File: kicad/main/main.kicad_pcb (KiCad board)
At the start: 2 copper layers, 39 x 35 mm, 17 parts, among them J3 Conn_01x07_Pin, J4 Conn_01x04_Pin, P1 USB_C_Plug_USB2.0, SW3 SW_Push, SW4 SW_Push, U1 HUSB237

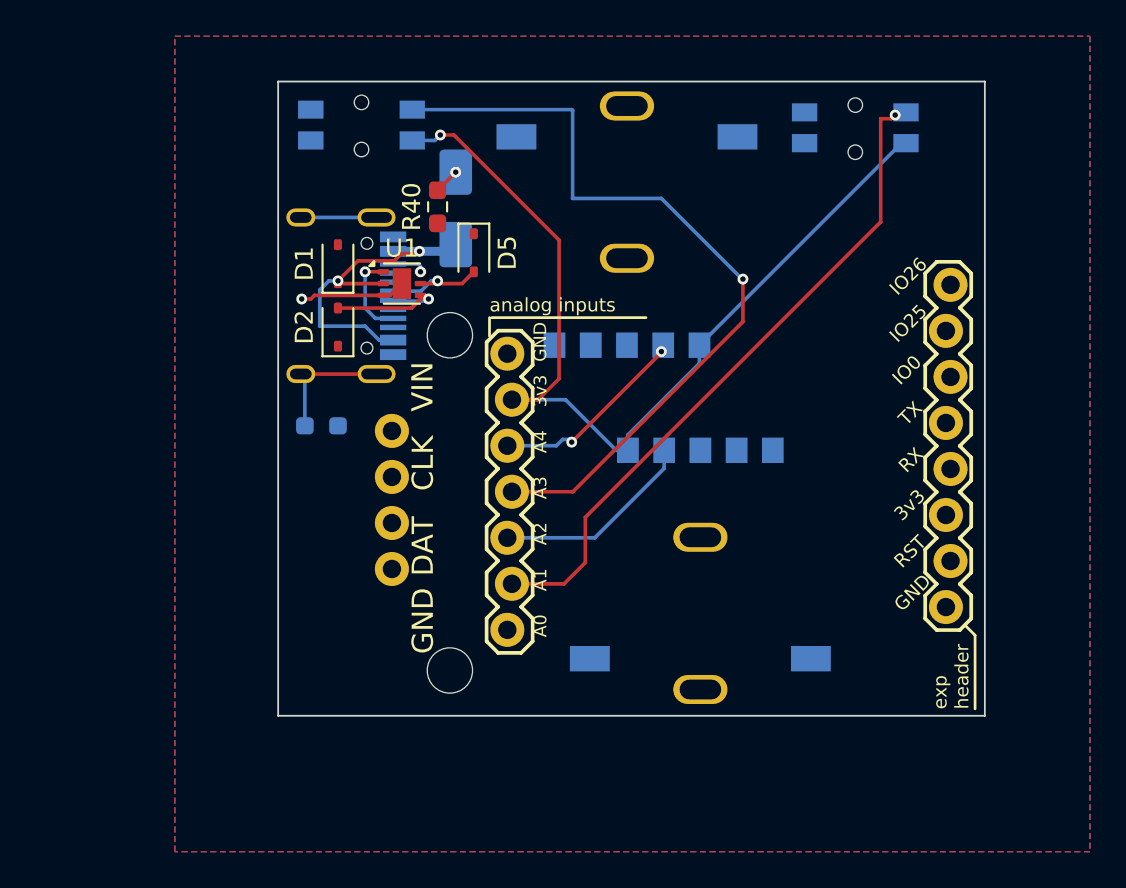
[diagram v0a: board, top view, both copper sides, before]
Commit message: Switches added
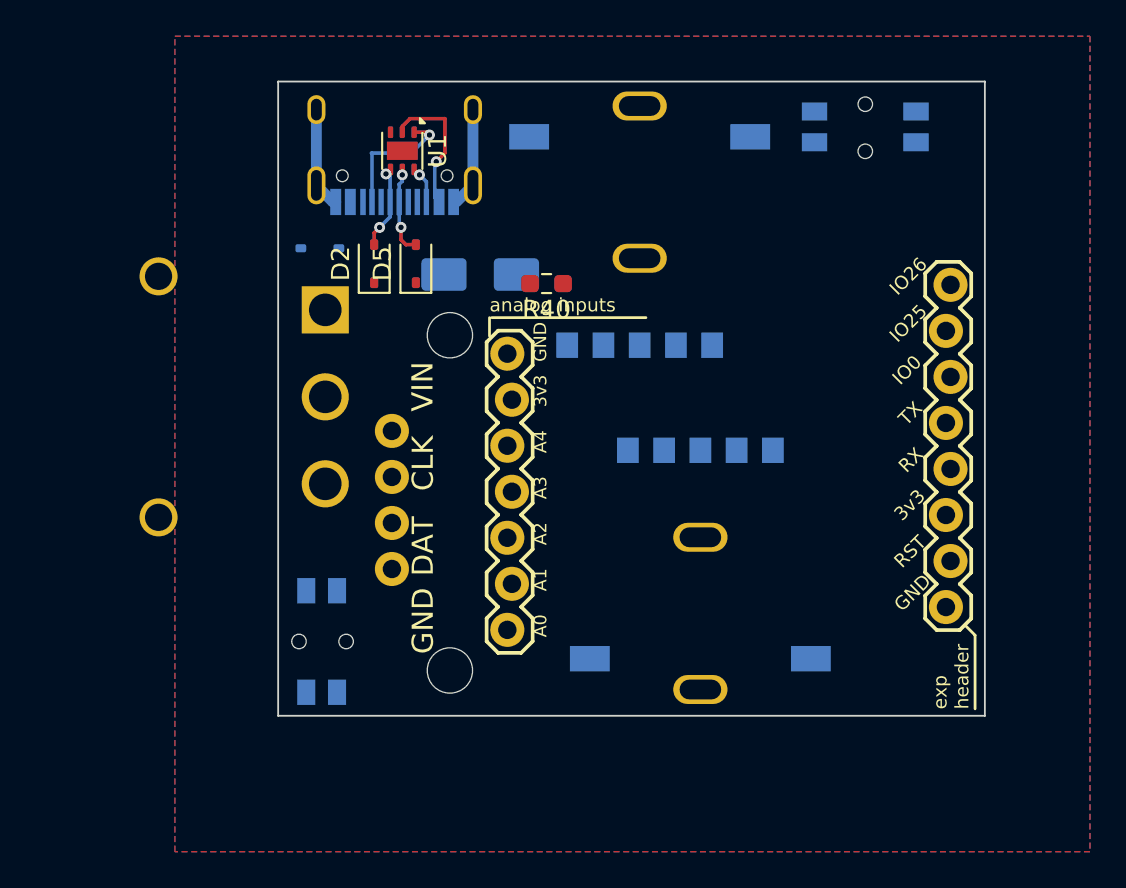
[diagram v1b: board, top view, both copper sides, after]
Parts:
- removed R39: 1M, Resistor_SMD:R_0603_1608Metric_Pad0.98x0.95mm_HandSolder
- added SW1: K3-1391B-51, easyeda2kicad:SW-TH_K3-1391B-51, B.Cu at (164.7, 92.4)
- D1: moved to B.Cu
- moved SW4 28.5 mm to (169.1, 105.9), turned to 90 degrees
- moved P1 10.1 mm to (173.1, 77.6), turned to 0 degrees
- moved R40 7.36 mm to (181.5, 86.2), turned to 180 degrees
- moved U1 7.33 mm to (173.6, 78.8), turned to -90 degrees
- moved D2 4.03 mm to (172.0, 85.0)
- moved D3 3.89 mm to (177.8, 85.7), turned to 0 degrees
- moved D5 3.26 mm to (174.3, 85.0), turned to 90 degrees
- moved D1 1.31 mm to (169.0, 84.2), turned to 180 degrees
- moved R1 0.70 mm to (186.7, 83.0)
- moved SW3 0.55 mm to (199.1, 77.5)
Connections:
- D3 pad 1: VIN -> VBUS
- D3 pad 2: VBUS -> Net-(D3-A)
- P1 pad S1: Net-(P1-SHIELD) -> GND
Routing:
- net +3V3: track 52.4 -> 0.00 mm, vias 1 -> 0
- net AIN3: track 43.9 -> 0.00 mm, vias 1 -> 0
- net AIN1: track 37.3 -> 0.00 mm, vias 1 -> 0
- net Net-(P1-SHIELD): track 11.3 -> 0.00 mm
- net AIN2: track 11.2 -> 0.00 mm
- net VBUS: track 18.9 -> 7.81 mm, vias 2 -> 1
- net AIN4: track 10.8 -> 0.00 mm, vias 2 -> 0
- net GND: track 5.88 -> 11.3 mm, vias 1 -> 0
- net D+: track 7.52 -> 4.80 mm, vias 1 -> 2
- net CC1: track 4.78 -> 7.24 mm
- net VIN: track 1.41 -> 0.00 mm, vias 1 -> 0
- net D-: track 5.91 -> 4.92 mm, vias 1 -> 2

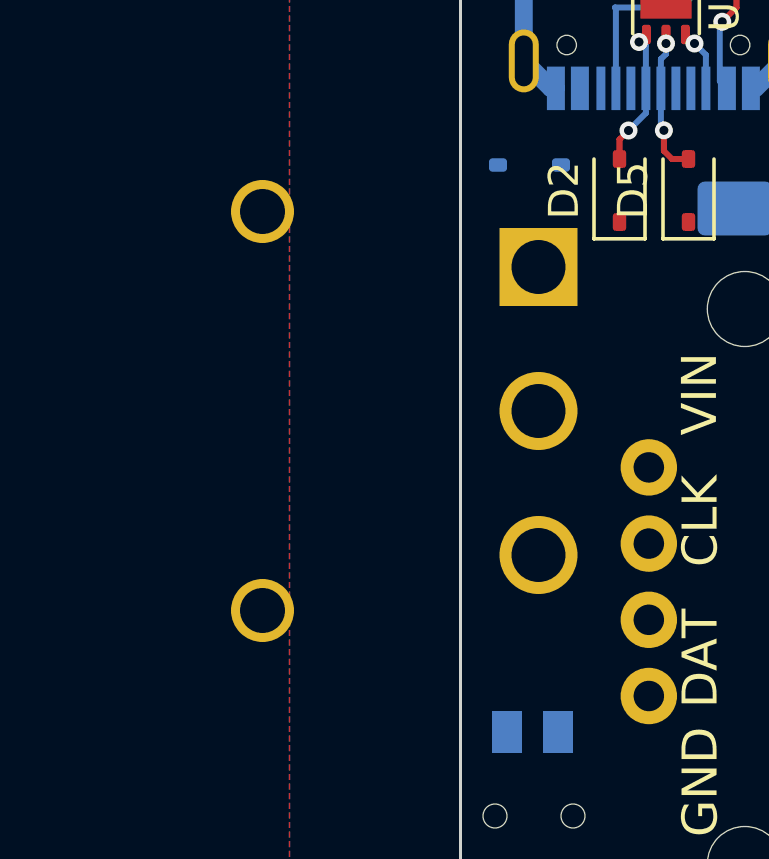
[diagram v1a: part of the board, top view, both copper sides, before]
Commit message: Added extra switched
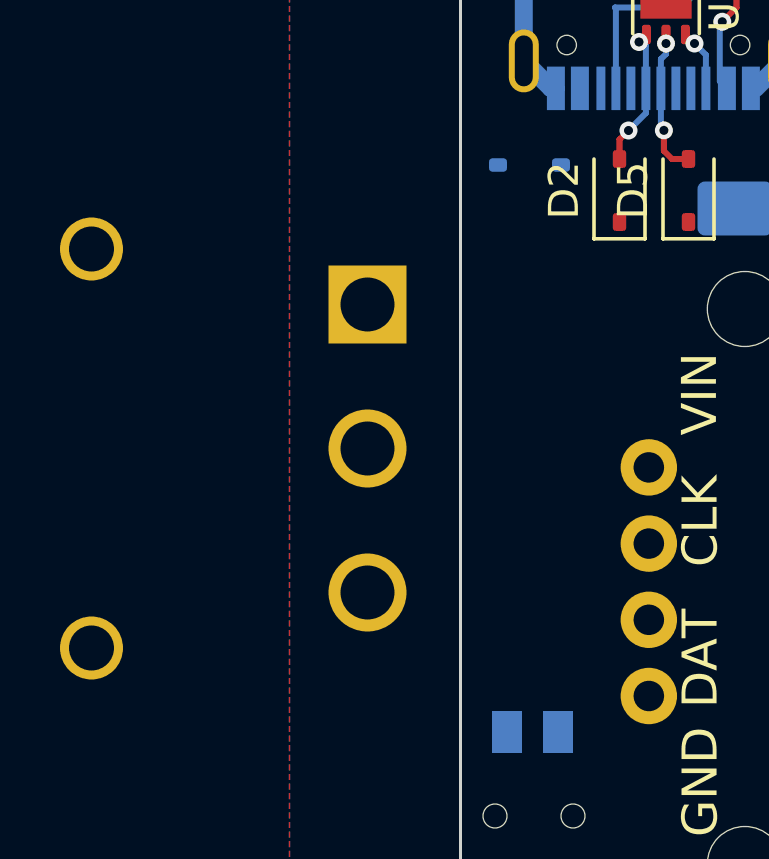
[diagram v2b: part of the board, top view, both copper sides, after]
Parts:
- moved SW1 5.84 mm to (159.0, 93.7)
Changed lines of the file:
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@@
 	(footprint "easyeda2kicad:SW-TH_K3-1391B-51"
 		(layer "B.Cu")
-		(at 164.7 92.4 90)
+		(at 159 93.65 90)
 		(property "Reference" "SW1"
 			(at 0 8.6 90)

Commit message: Finished design
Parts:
- removed J1: , 1X08_LOCK_513
- added C1: 1u, Capacitor_SMD:C_0805_2012Metric, F.Cu at (178.9, 79.0)
- added J2: Conn_01x02, Connector_PinHeader_2.54mm:PinHeader_1x02_P2.54mm_Vertical, F.Cu at (179.0, 84.5)
- added U2: ZX-PH2.0-WT4P, easyeda2kicad:CONN-SMD_4P-P2.00_C2001RS10411M0101RC, B.Cu at (166.4, 102.2)
- D1: moved to F.Cu
- SW1: value K3-1391B-51 -> MK-12C03-G015; footprint easyeda2kicad:SW-TH_K3-1391B-51 -> easyeda2kicad:SW-SMD_MK-12C03-G015
- moved SW4 29.8 mm to (176.2, 76.9), turned to 0 degrees
- moved R40 8.11 mm to (175.4, 91.5)
- moved P1 7.78 mm to (166.1, 80.8), turned to 90 degrees
- moved D5 7.56 mm to (173.9, 77.5), turned to 180 degrees
- moved U1 7.21 mm to (166.5, 80.3), turned to 0 degrees
- moved SW1 5.21 mm to (163.5, 91.0)
- moved D2 4.73 mm to (174.4, 81.0), turned to 180 degrees
- moved D1 4.71 mm to (164.4, 83.0)
- moved D3 3.54 mm to (175.5, 83.0), turned to -90 degrees
- moved R1 2.75 mm to (189.4, 82.9)
- moved SW3 2.10 mm to (201.2, 77.5)
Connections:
- SW1 pad 2: VBUS -> VIN
- SW1 pad 3: VIN -> VBUS
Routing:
- net +3V3: track 0.00 -> 56.0 mm
- net AIN1: track 0.00 -> 41.9 mm, vias 0 -> 1
- net AIN3: track 0.00 -> 33.8 mm, vias 0 -> 1
- net VBUS: track 7.81 -> 40.7 mm, vias 1 -> 6
- net VIN: track 0.00 -> 25.5 mm
- net SCK_OUT: track 0.00 -> 18.6 mm
- net AIN4: track 0.00 -> 14.4 mm, vias 0 -> 2
- net MOSI_OUT: track 0.00 -> 12.7 mm
- net AIN2: track 0.00 -> 11.9 mm
- net GND: track 11.3 -> 20.0 mm, vias 0 -> 56
- net D-: track 4.92 -> 10.2 mm, vias 2 -> 1
- net Net-(D3-A): track 0.00 -> 3.71 mm
- net D+: track 4.80 -> 8.06 mm, vias 2 -> 1
- net CC1: track 7.24 -> 8.69 mm
- net CC2: track 2.08 -> 3.06 mm
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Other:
- board size 39 x 35 mm -> 44.5 x 35 mm
- board text added: "+"
- board text removed: "IO0"
- board text removed: "IO25"
- board text removed: "IO26"
- board text removed: "RST"
- board text removed: "RX"
- board text removed: "TX"
- board text removed: "exp header"

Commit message: Finished design added more vias
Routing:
- net GND: vias 56 -> 59

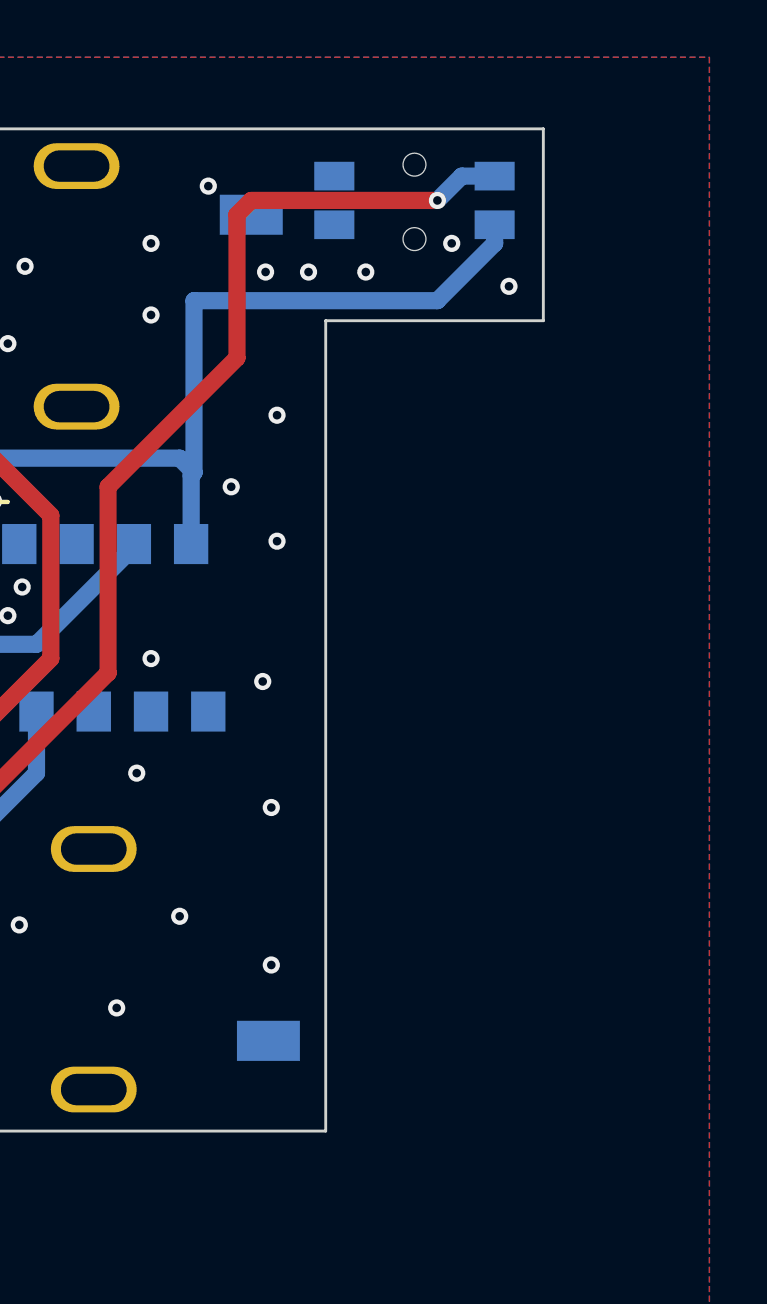
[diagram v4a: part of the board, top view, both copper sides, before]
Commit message: Rotated switch
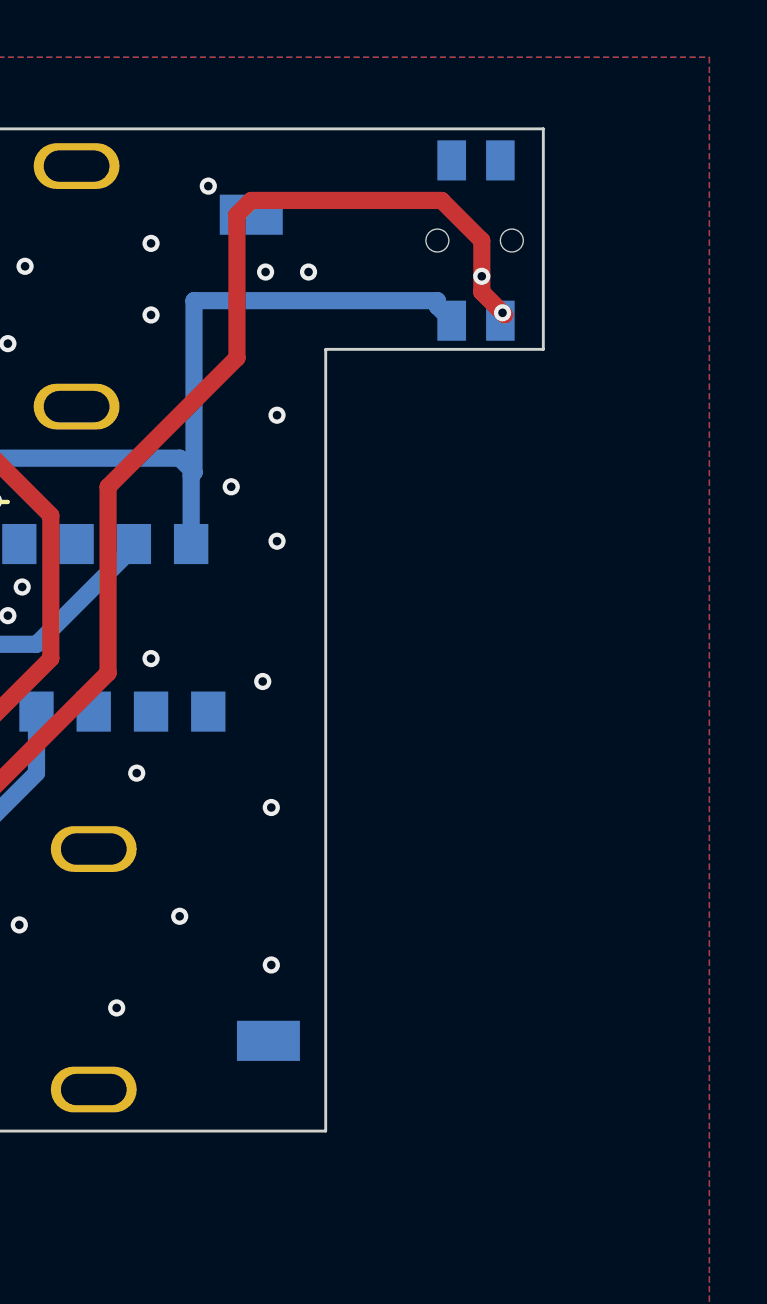
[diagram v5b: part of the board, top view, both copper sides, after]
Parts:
- moved SW3 2.50 mm to (203.3, 78.9), turned to -90 degrees
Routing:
- net AIN1: track 41.9 -> 44.6 mm, vias 1 -> 2
- net +3V3: track 56.0 -> 53.4 mm
- net GND: vias 59 -> 56
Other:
- outline, holes or cut-outs redrawn

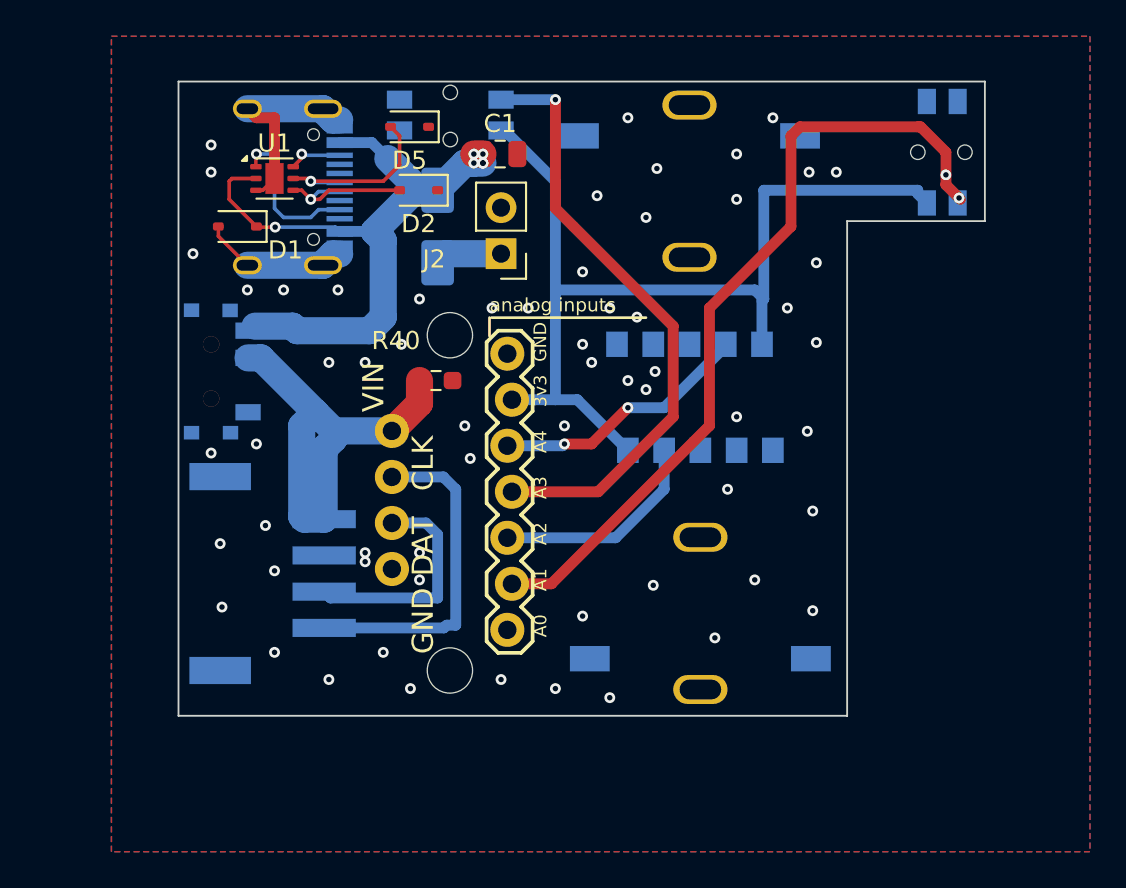
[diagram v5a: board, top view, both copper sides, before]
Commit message: Increased trace widths
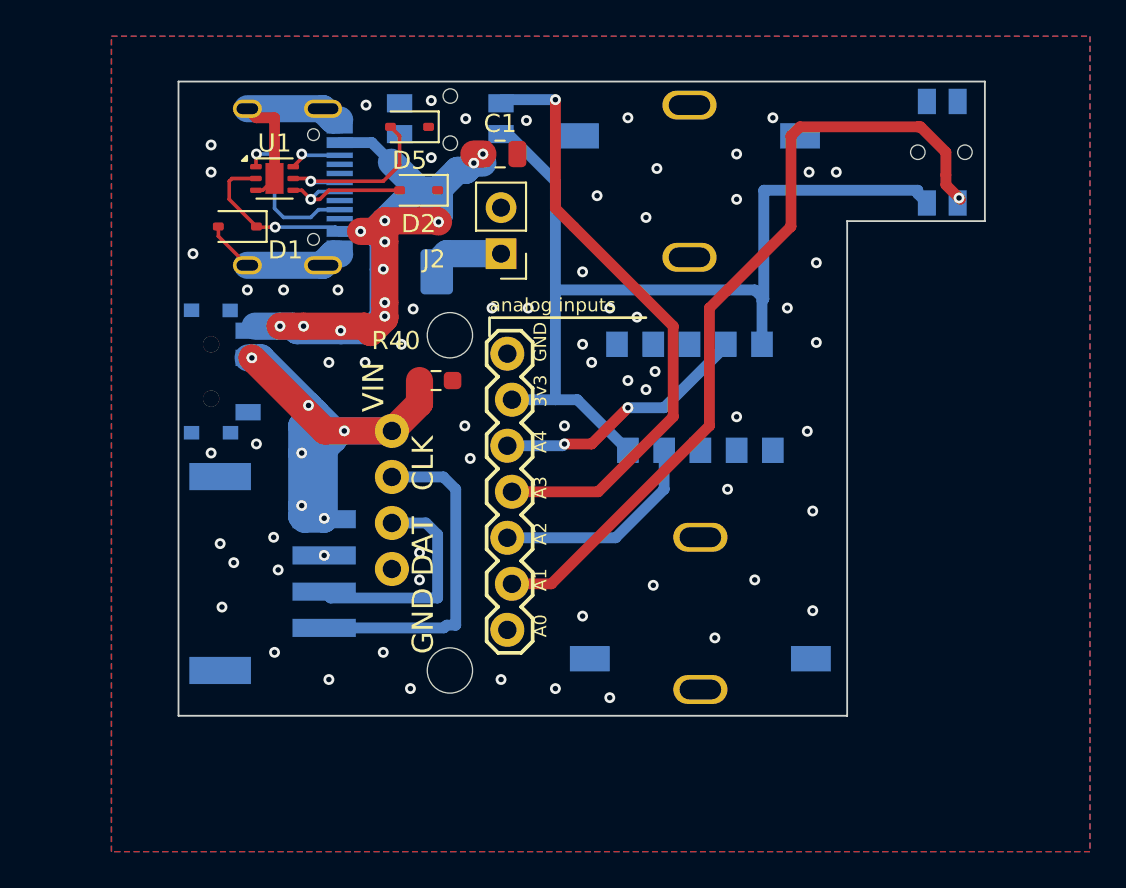
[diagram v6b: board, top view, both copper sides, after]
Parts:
- moved D3 0.50 mm to (175.4, 83.5)
- moved SW4 0.20 mm to (176.2, 77.1)
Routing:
- net VBUS: track 40.7 -> 56.6 mm, vias 6 -> 13
- net VIN: track 25.5 -> 34.9 mm, vias 0 -> 6
- net GND: vias 56 -> 61
- net AIN1: vias 2 -> 1

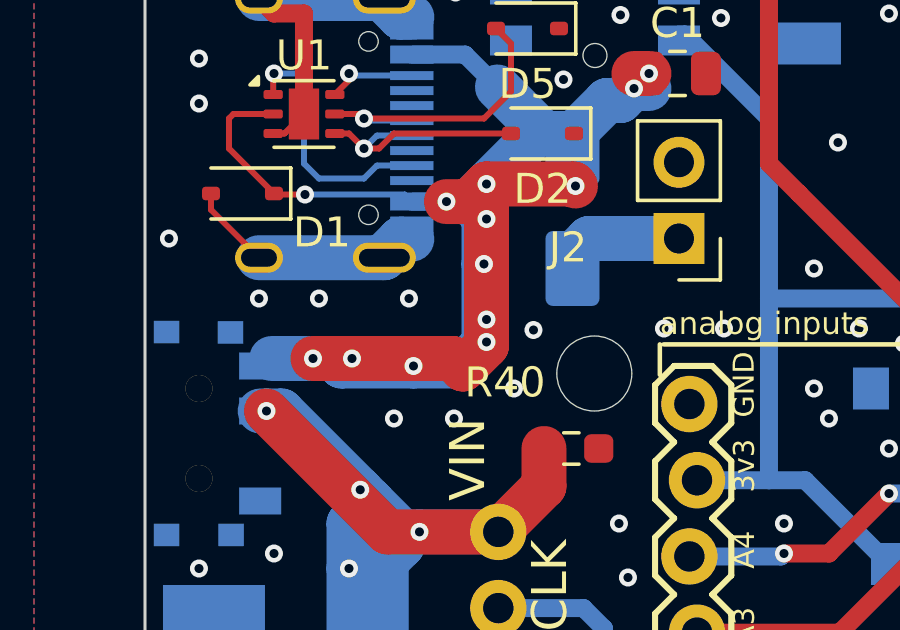
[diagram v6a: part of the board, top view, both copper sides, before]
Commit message: Increased trace widths
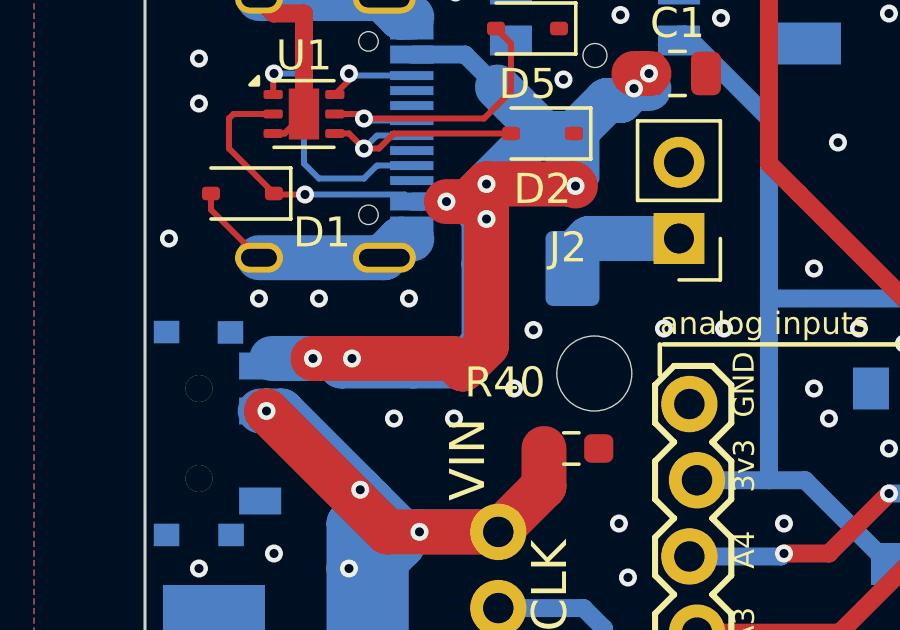
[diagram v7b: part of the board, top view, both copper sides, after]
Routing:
- net VBUS: vias 13 -> 9
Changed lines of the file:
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@@
-	)
-	(via
-		(at 172.585 87.2)
-		(size 0.6)
-		(drill 0.3)
-		(layers "F.Cu" "B.Cu")
-		(net 11)
 	)
 	(via
@@
 	)
 	(via
-		(at 172.585 87.95)
-		(size 0.6)
-		(drill 0.3)
-		(layers "F.Cu" "B.Cu")
-		(net 11)
-	)
-	(via
 		(at 166.8 88.5)
 		(size 0.6)
@@
 	(via
 		(at 172.585 83.85)
-		(size 0.6)
-		(drill 0.3)
-		(layers "F.Cu" "B.Cu")
-		(net 11)
-	)
-	(via
-		(at 170.15 88.75)
 		(size 0.6)
 		(drill 0.3)
@@
 		(size 0.6)
 		(drill 0.3)
-		(layers "F.Cu" "B.Cu")
-		(net 11)
-	)
-	(via
-		(at 172.5 85.35)
-		(size 0.6)
-		(drill 0.3)
